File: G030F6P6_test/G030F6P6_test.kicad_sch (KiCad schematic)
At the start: 28 parts, among them J3 USB_C_Receptacle_USB2.0, U1 CH343P, U2 STM32G030FxP, U3 XC6206P332MR

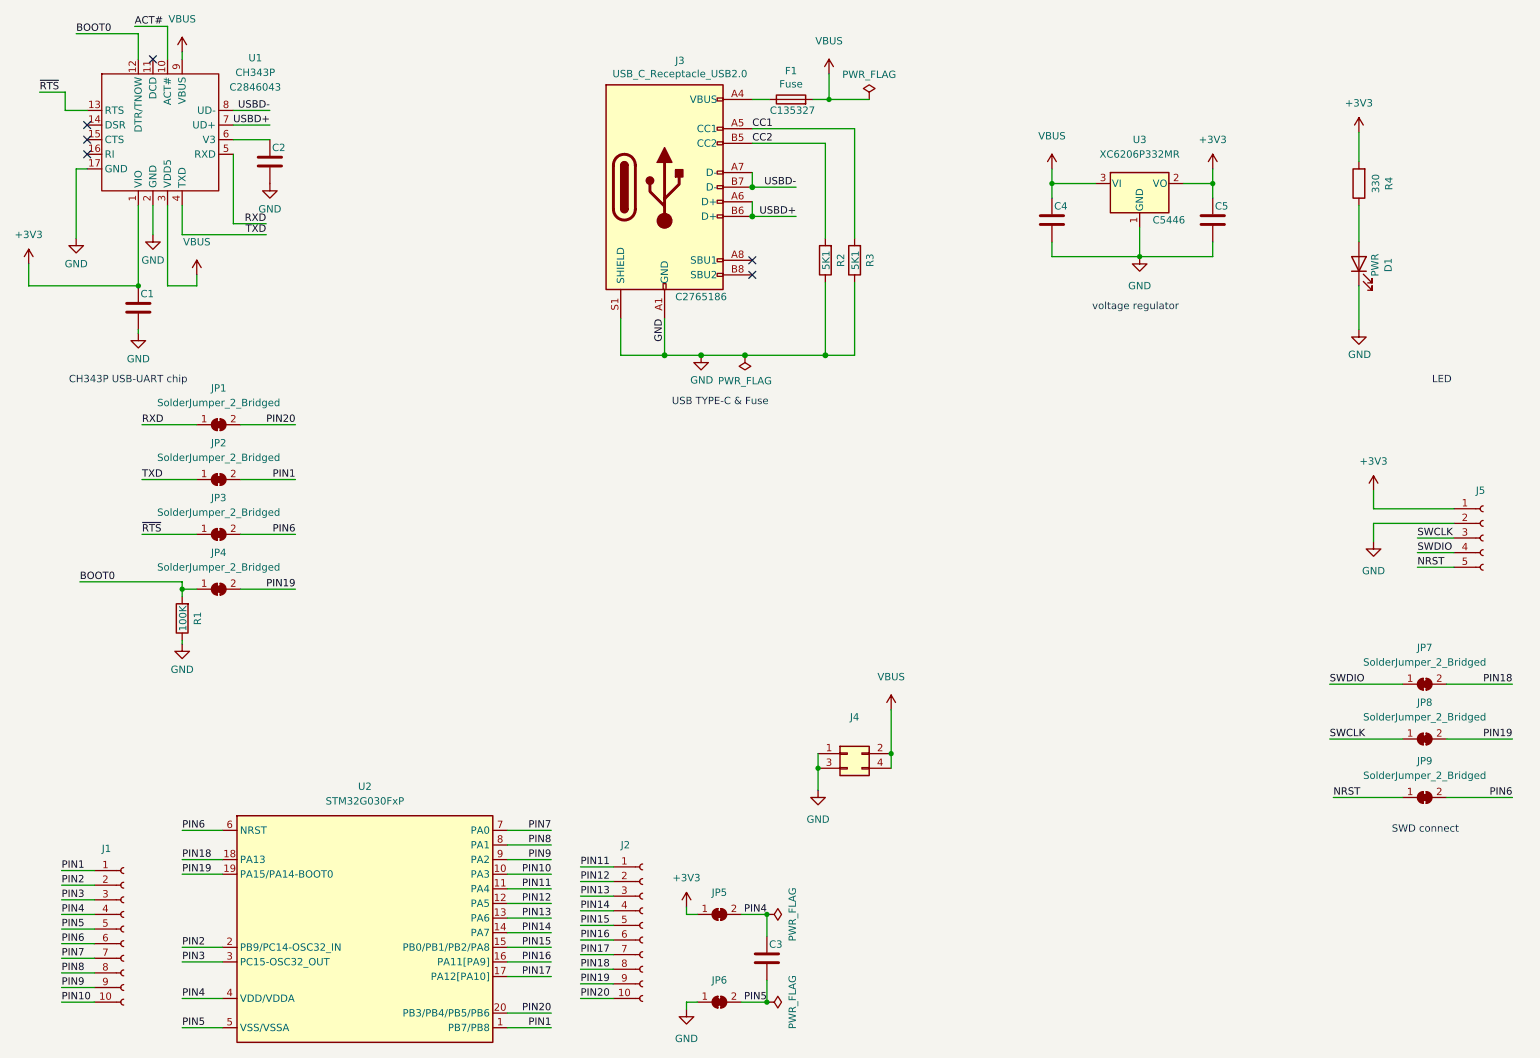
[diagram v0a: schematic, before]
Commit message: 軟體升級KiCAD V7
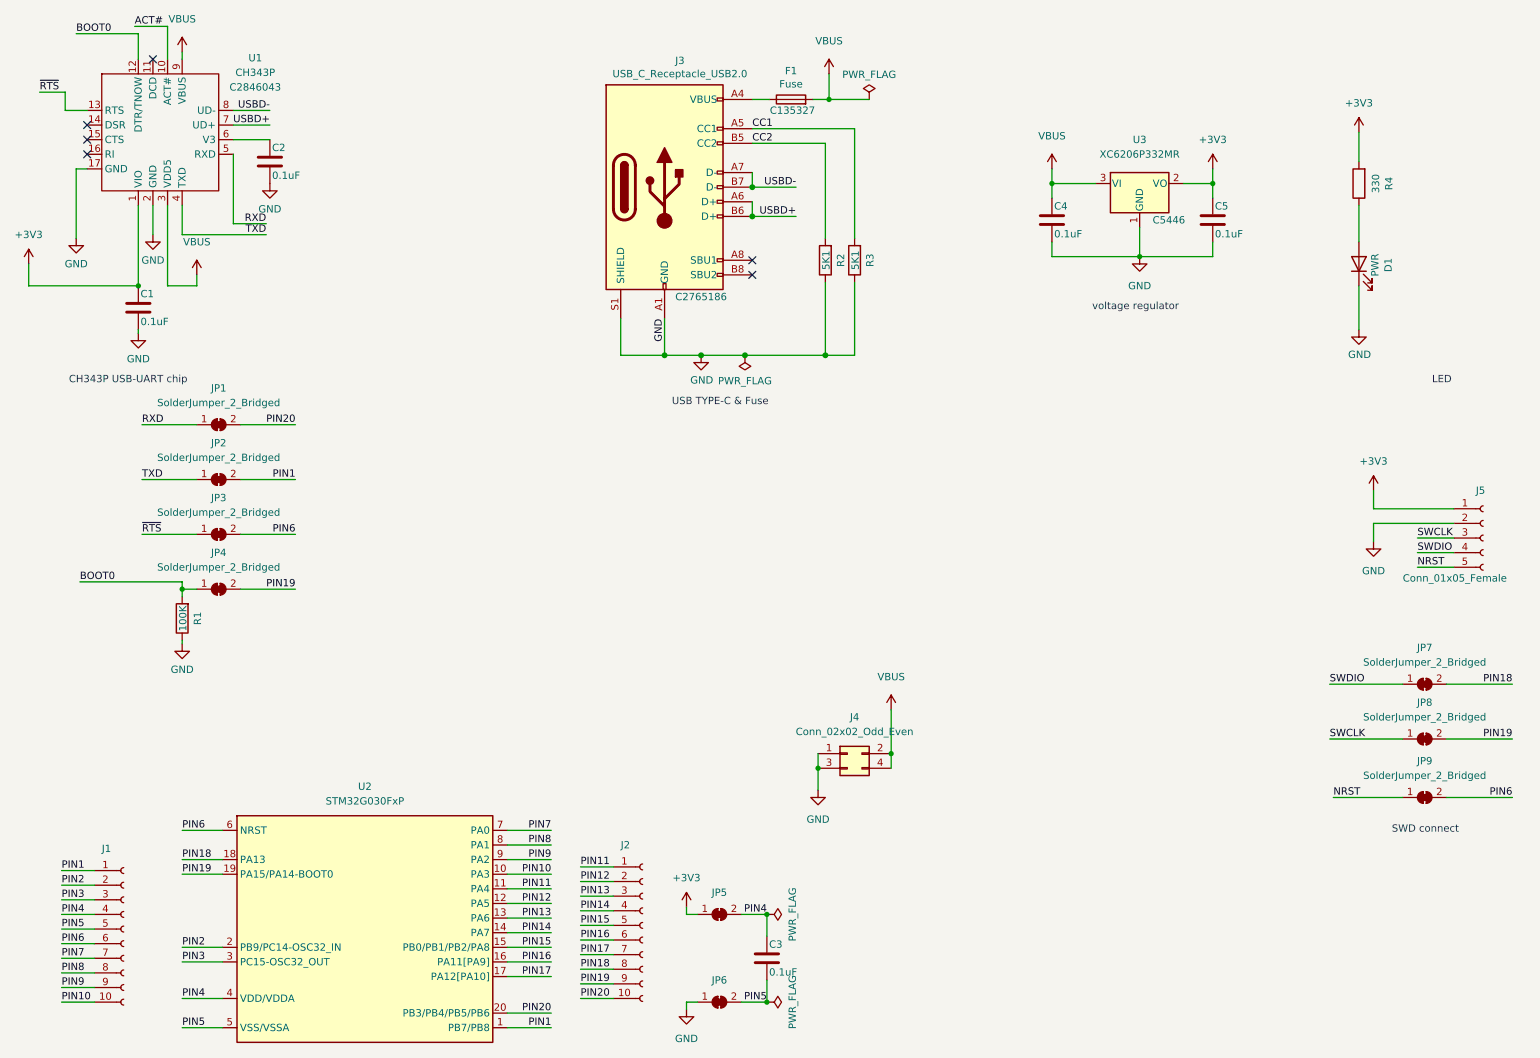
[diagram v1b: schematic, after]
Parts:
- C1, C2, C3, C4, C5: value (none) -> 0.1uF; footprint (none) -> Capacitor_SMD:C_0805_2012Metric
- J1, J2: value (none) -> Conn_01x10_Female; footprint (none) -> Connector_PinHeader_2.54mm:PinHeader_1x10_P2.54mm_Vertical
- J4: value (none) -> Conn_02x02_Odd_Even; footprint (none) -> Connector_PinSocket_2.54mm:PinSocket_2x02_P2.54mm_Vertical
- J5: value (none) -> Conn_01x05_Female; footprint (none) -> Connector_PinHeader_2.54mm:PinHeader_1x05_P2.54mm_Vertical
